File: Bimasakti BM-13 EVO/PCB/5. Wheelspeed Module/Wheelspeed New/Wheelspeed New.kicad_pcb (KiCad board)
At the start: 2 copper layers, 32 x 46.5 mm, 21 parts, among them J3 Conn_01x15_Pin, J4 Conn_01x15_Pin, U1 ESP32-C3_SUPERMINI_TH, U2 LM393

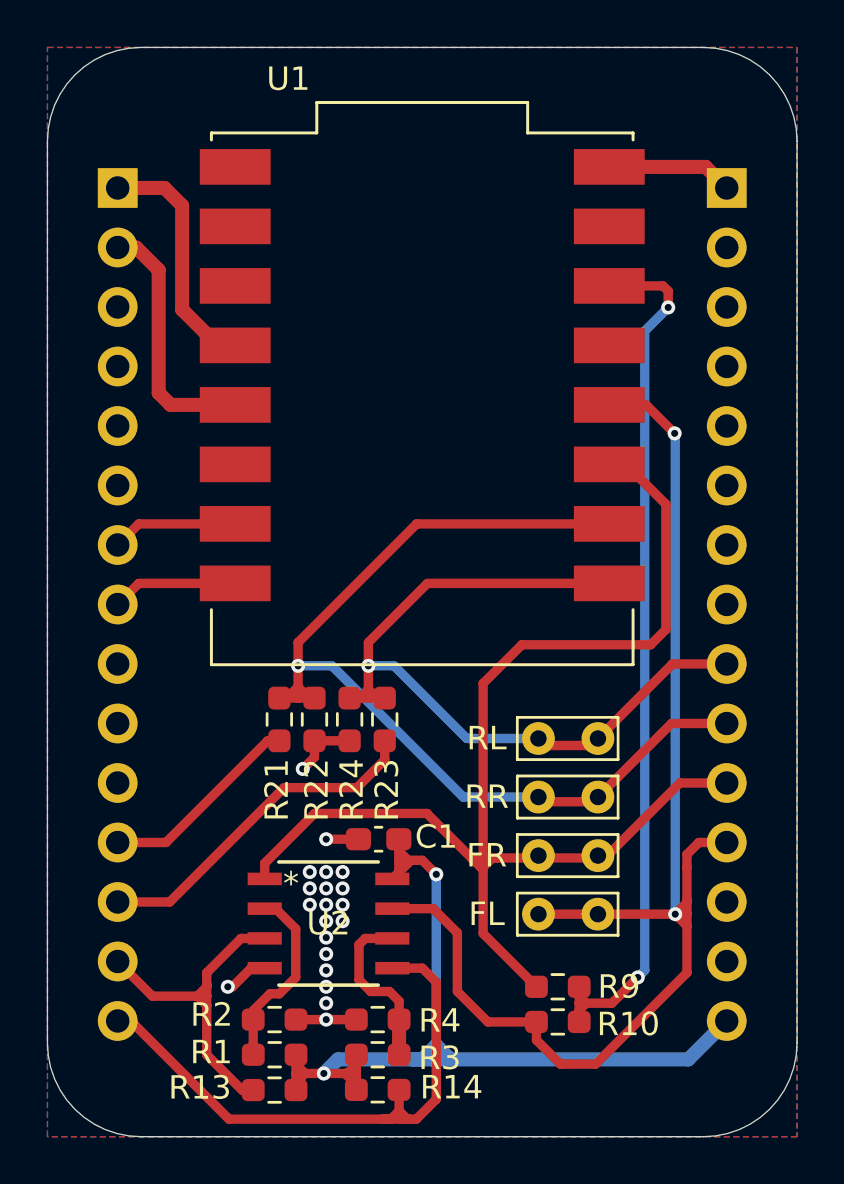
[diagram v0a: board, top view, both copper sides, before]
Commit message: tambah level shifter karena mau dibuat traction control
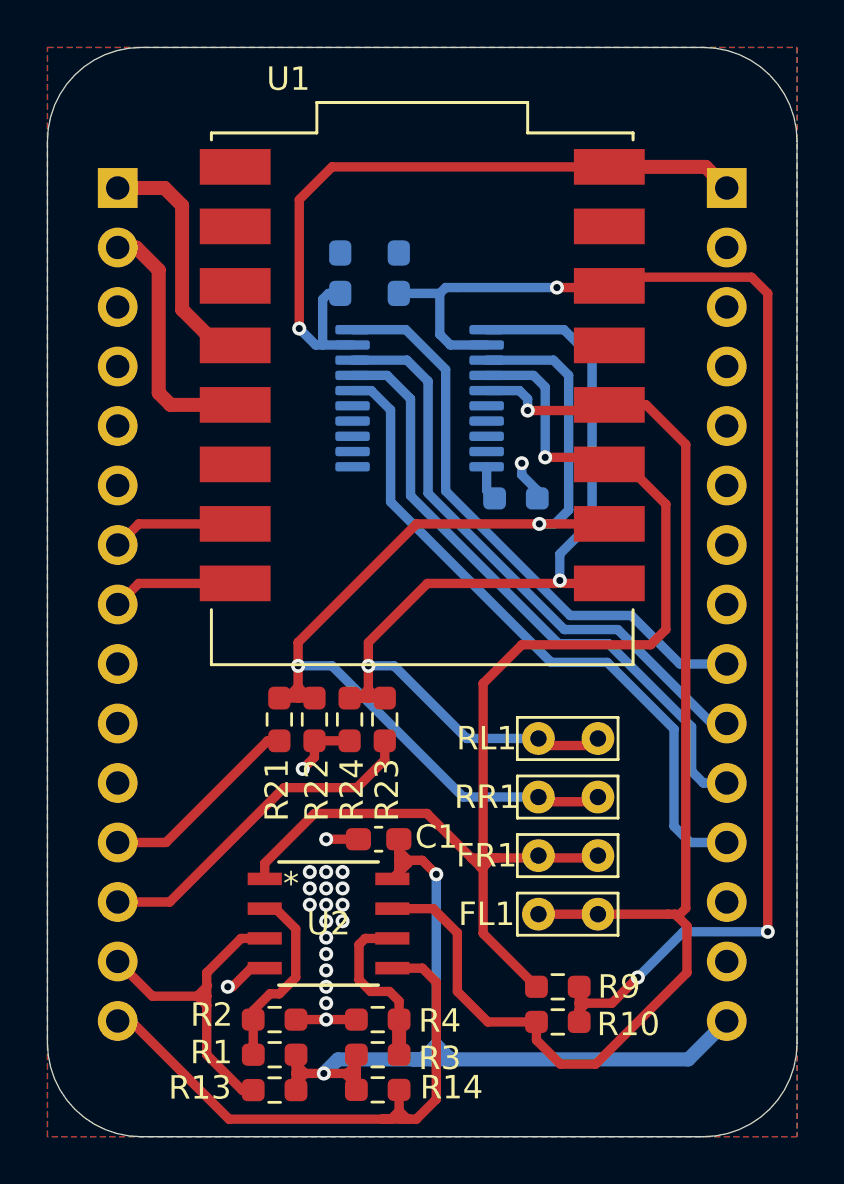
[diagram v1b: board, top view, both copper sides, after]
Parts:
- added C2: 0.1uF, Capacitor_SMD:C_0603_1608Metric_Pad1.08x0.95mm_HandSolder, B.Cu at (114.0, 111.6)
- added C3: 0.1uF, Capacitor_SMD:C_0603_1608Metric_Pad1.08x0.95mm_HandSolder, B.Cu at (111.5, 111.6)
- added R5: 10K, Resistor_SMD:R_0603_1608Metric_Pad0.98x0.95mm_HandSolder, B.Cu at (119.0, 121.2)
- added U3: TXS0108EPW, Package_SO:TSSOP-20_4.4x6.5mm_P0.65mm, B.Cu at (114.9, 117.0)
- renumbered FL to FL1, FR to FR1, RL to RL1, RR to RR1
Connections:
- J4 pad 10: /WS_RR_Signal -> /WS_RR_Signal_5V
- J4 pad 11: /WS_FR_Signal -> /WS_FR_Signal_5V
- J4 pad 12: /WS_FL_Signal -> /WS_FL_Signal_5V
- J4 pad 9: /WS_RL_Signal -> /WS_RL_Signal_5V
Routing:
- net /WS_FL_Signal_5V: track 0.00 -> 28.7 mm
- net /WS_FR_Signal_5V: track 0.00 -> 26.7 mm
- net /WS_RR_Signal_5V: track 0.00 -> 25.2 mm
- net /WS_RL_Signal_5V: track 0.00 -> 24.9 mm
- net +5V: track 5.39 -> 30.1 mm, vias 0 -> 1
- net +3.3V: track 38.6 -> 60.1 mm, vias 2 -> 3
- net /WS_RL_Signal: track 36.0 -> 44.4 mm, vias 1 -> 2
- net /WS_RR_Signal: track 43.8 -> 48.0 mm, vias 1 -> 2
- net /WS_FR_Signal: track 55.9 -> 58.0 mm, vias 0 -> 1
- net GND: track 8.76 -> 10.5 mm, vias 20 -> 21
- net Net-(U3-OE): track 0.00 -> 1.49 mm
- net /WS_FL_Signal: track 57.7 -> 57.8 mm, vias 2 -> 1
